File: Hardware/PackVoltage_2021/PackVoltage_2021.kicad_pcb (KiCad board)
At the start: 2 copper layers, 152.4 x 177.8 mm, 139 parts, among them J3V1 Test_Point, J5V1 Test_Point, Q1 BUK7M8R5-40HX, Q10 BUK7M8R5-40HX, Q2 BUK7M8R5-40HX, Q3 BUK7M8R5-40HX, Q4 BUK7M8R5-40HX, Q5 BUK7M8R5-40HX, Q6 BUK7M8R5-40HX, Q7 BUK7M8R5-40HX, Q8 BUK7M8R5-40HX, Q9 BUK7M8R5-40HX, U1 LT1910, U10 INA281, U12 OKI-78SR-3.3_1.5-W36-C, U13 OKI-78SR-5_1.5-W36-C, U14 LT1910, U15 LT1910, U16 LT1910, U17 INA281, U18 INA281, U19 INA281, U2 LT1910, U20 LT1910, U21 LT1910, U22 INA281, U23 INA281, U24 TM4C129E_Launchpad, U3 LT1910, U4 INA281, U5 INA281, U6 INA281, U7 LT1910, U8 LT1910, U9 INA281

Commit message: rearranged components
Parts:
- removed the REF** at (172.7, 67.8)
- removed the REF** at (168.9, 156.7)
- added REF**: 4_40_Hole, MRDT_Drill_Holes:4_40_Hole, F.Cu at (169.4, 63.2)
- added REF**: 4_40_Hole, MRDT_Drill_Holes:4_40_Hole, F.Cu at (169.4, 156.7)
- moved R10 196.0 mm to (168.9, 19.6)
- moved U5 184.2 mm to (156.5, 32.0)
- moved U7 148.9 mm to (176.5, 22.4)
- moved R9 24.2 mm to (100.8, 33.8), turned to 180 degrees
- moved D5 19.6 mm to (100.8, 31.5), turned to 180 degrees
- moved R3 13.5 mm to (93.2, 19.3), turned to 90 degrees
- moved U3 11.2 mm to (102.9, 25.9)
- moved J3V1 8.13 mm to (89.9, 71.1)
- moved Q3 7.37 mm to (110.2, 26.4), turned to 270 degrees
- moved C7 5.45 mm to (95.5, 12.2)
- moved R6 1.61 mm to (114.6, 21.6)
- moved U6 1.61 mm to (104.1, 14.5), turned to 90 degrees
- moved C19 0.80 mm to (83.2, 66.5)
- moved D13 0.80 mm to (82.3, 63.0)
- moved R18 0.80 mm to (83.2, 59.7)
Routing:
- net +3V3: track 137.8 -> 111.5 mm

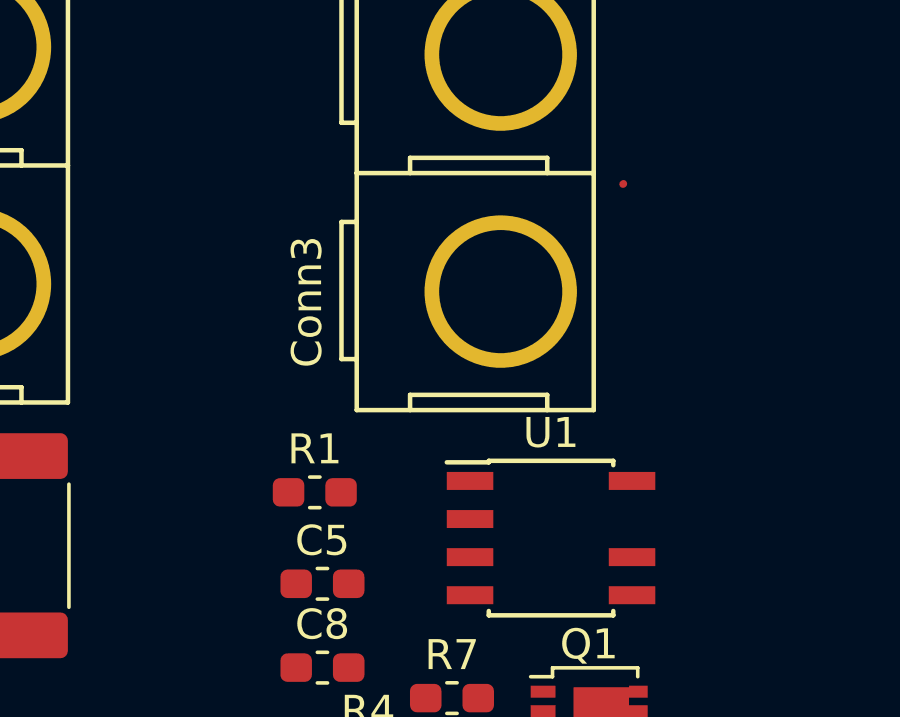
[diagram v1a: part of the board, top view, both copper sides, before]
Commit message: rearranged components (layout)
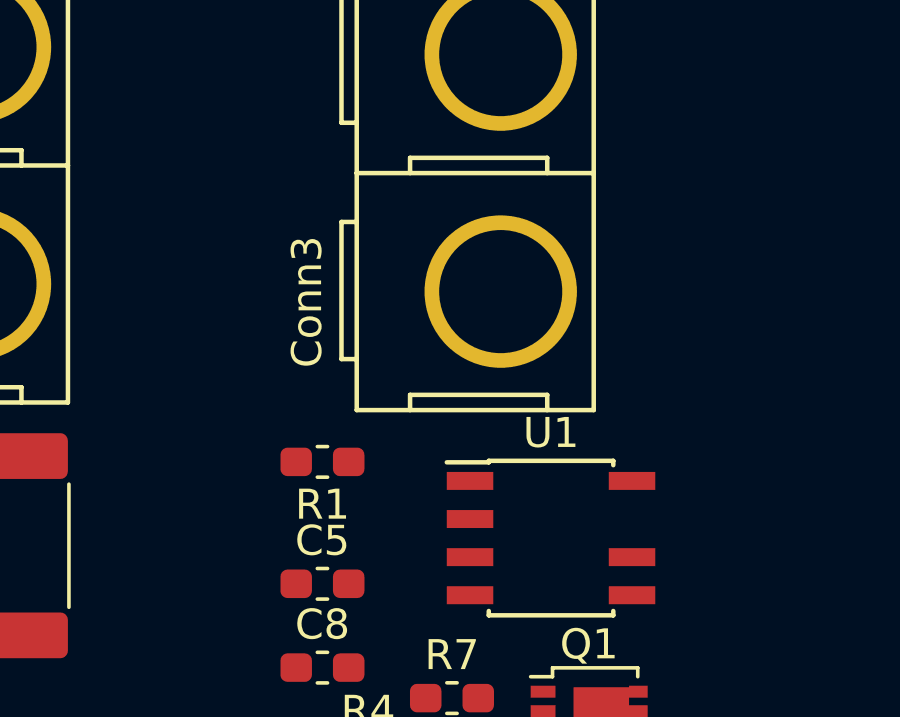
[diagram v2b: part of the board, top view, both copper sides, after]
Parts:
- moved R1 1.05 mm to (124.7, 18.8), turned to 180 degrees

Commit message: circuit, deletes
made circuit to copy across board (hopefully);
deleted old traces that "aren't wide enough"
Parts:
- removed J3V1, J5V1: Test_Point, TestPoint:TestPoint_Pad_2.5x2.5mm
- removed REF** (x4): 4_40_Hole, MRDT_Drill_Holes:4_40_Hole
- moved U4 21.1 mm to (129.3, 14.2), turned to 90 degrees
- moved C8 17.3 mm to (127.8, 42.7), turned to 270 degrees
- moved D3 17.1 mm to (143.0, 17.8), turned to 270 degrees
- moved D5 16.0 mm to (113.5, 21.8), turned to 270 degrees
- moved R4 15.8 mm to (139.4, 21.1), turned to 90 degrees
- moved Conn10 15.3 mm to (208.8, 4.83)
- moved C7 15.2 mm to (102.6, 25.7), turned to 0 degrees
- moved R7 14.9 mm to (143.0, 21.6), turned to 90 degrees
- moved R9 14.8 mm to (112.5, 24.6), turned to 0 degrees
- moved Conn9 10.4 mm to (184.9, 4.83)
- moved U1 8.64 mm to (124.5, 24.9), turned to 270 degrees
- moved Q3 8.29 mm to (106.4, 33.8)
- moved R3 8.18 mm to (99.8, 14.5)
- moved Conn7 7.41 mm to (161.0, 4.83)
- moved C19 7.37 mm to (90.6, 66.3)
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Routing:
- net /DriveCTL: track 125.6 -> 0.00 mm
- net /ExtraCTL: track 123.7 -> 0.00 mm
- net /CameraCTL: track 122.5 -> 0.00 mm
- net /BuckCTL: track 117.5 -> 0.08 mm
- net /NavBoardCTL: track 110.9 -> 0.00 mm
- net /GimbalActCTL: track 110.1 -> 0.00 mm
- net /GimbalLogCTL: track 108.3 -> 0.00 mm
- net /AuxActCTL: track 106.4 -> 0.00 mm
- net /AuxLogCTL: track 104.5 -> 0.00 mm
- net /MultimediaLogCTL: track 103.6 -> 0.90 mm
- net /MultimediaActCTL: track 102.7 -> 0.00 mm
- net /GimbalSense: track 81.9 -> 0.00 mm
- net /LowCurrentSense: track 75.7 -> 0.00 mm
- net +3V3: track 111.5 -> 36.8 mm, vias 0 -> 2
- net /MultimediaSense: track 69.5 -> 0.00 mm
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- added copper zone on F.Cu, net /Anderson_M1
- added copper zone on F.Cu, net /Anderson_M2
- added copper zone on F.Cu, net Net-(C10-Pad1)
- added copper zone on F.Cu, net Net-(Q1-Pad1)
- added copper zone on F.Cu, net Net-(Q3-Pad1)
- removed copper zone on B.Cu, net GND

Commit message: did a thing
arranged circuit for motor 2
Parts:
- moved C13 206.5 mm to (158.5, 42.7), turned to 270 degrees
- moved C29 188.4 mm to (173.0, 42.7), turned to 270 degrees
- moved C9 16.6 mm to (143.5, 42.7), turned to 270 degrees
- moved R4 14.0 mm to (125.5, 21.3)
- moved R7 13.8 mm to (129.5, 24.6), turned to 180 degrees
- moved U4 13.5 mm to (117.1, 20.1)
- moved D3 13.0 mm to (130.6, 21.6)
- moved Q1 12.7 mm to (123.6, 33.8)
- moved Conn3 11.7 mm to (125.5, 4.70)
- moved C5 10.3 mm to (118.6, 25.9), turned to 0 degrees
- moved U1 8.99 mm to (118.4, 31.5)
- moved R1 7.85 mm to (116.6, 14.5)
- moved C8 0.51 mm to (127.3, 42.7)
- moved Q3 0.13 mm to (106.6, 33.8)
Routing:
- net Net-(Q1-Pad4): track 0.00 -> 8.09 mm, vias 0 -> 2
- added copper zone on F.Cu, net (none)
- removed copper zone on F.Cu, net /Anderson_M2
- removed copper zone on F.Cu, net Net-(Q1-Pad1)

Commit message: uhh more circuits
finished top circuits on layout, fixed two resistors in schematic
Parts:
- moved C11 209.8 mm to (153.0, 25.9)
- moved D4 198.9 mm to (146.9, 21.6), turned to 270 degrees
- moved Q4 198.8 mm to (156.5, 33.8), turned to 270 degrees
- moved R14 192.5 mm to (162.1, 24.6)
- moved R28 192.2 mm to (166.1, 14.5), turned to 90 degrees
- moved C27 189.8 mm to (169.4, 25.9)
- moved R32 189.5 mm to (178.6, 24.6)
- moved D17 186.0 mm to (179.6, 21.3), turned to 270 degrees
- moved U9 182.3 mm to (150.4, 20.1), turned to 90 degrees
- moved D6 178.0 mm to (163.1, 21.3), turned to 270 degrees
- moved R12 175.9 mm to (158.0, 21.3), turned to 90 degrees
- moved Q9 166.6 mm to (173.0, 33.8), turned to 270 degrees
- moved U22 166.2 mm to (166.1, 20.1), turned to 90 degrees
- moved R30 162.5 mm to (174.5, 21.3), turned to 90 degrees
- moved U20 161.0 mm to (167.9, 31.5), turned to 270 degrees
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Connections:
- R14 pad 1: /Anderson_M4 -> Net-(Q4-Pad1)
- R32 pad 1: /Anderson_D1 -> Net-(Q9-Pad1)
- U24 pad PD2: /Current_Sensor_M3 -> /Driver_M3
- U24 pad PP0: /Driver_M3 -> /Current_Sensor_M3
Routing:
- net +3V3: track 36.8 -> 137.1 mm, vias 2 -> 7
- net /Current_Sensor_M3: track 0.00 -> 83.4 mm, vias 0 -> 2
- net /Driver_M3: track 0.00 -> 74.6 mm, vias 0 -> 2
- net /Current_Sensor_M2: track 0.00 -> 70.2 mm, vias 0 -> 2
- net +5V: track 25.5 -> 94.9 mm, vias 1 -> 3
- net /Driver_M2: track 0.00 -> 62.0 mm, vias 0 -> 2
- net Net-(R2-Pad1): track 0.00 -> 22.0 mm, vias 0 -> 4
- net Net-(R28-Pad1): track 0.00 -> 21.5 mm, vias 0 -> 4
- net Net-(R1-Pad1): track 0.00 -> 20.4 mm, vias 0 -> 4
- net Net-(R10-Pad1): track 0.00 -> 20.4 mm, vias 0 -> 4
- net Net-(Q9-Pad1): track 0.00 -> 10.7 mm, vias 0 -> 2
- net Net-(Q1-Pad1): track 0.00 -> 10.2 mm, vias 0 -> 2
- net Net-(Q2-Pad1): track 0.00 -> 9.99 mm, vias 0 -> 2
- net Net-(Q4-Pad1): track 0.00 -> 9.62 mm, vias 0 -> 2
- net Net-(Q2-Pad4): track 0.00 -> 7.93 mm, vias 0 -> 2
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- added copper zone on F.Cu, net /Anderson_D1
- added copper zone on F.Cu, net /Anderson_M2
- added copper zone on F.Cu, net /Anderson_M3
- added copper zone on F.Cu, net Net-(C13-Pad1)
- added copper zone on F.Cu, net Net-(C29-Pad1)
- added copper zone on F.Cu, net Net-(C8-Pad1)
- added copper zone on F.Cu, net Net-(C9-Pad1)
- added copper zone on F.Cu, net Net-(Q1-Pad1)
- added copper zone on F.Cu, net Net-(Q2-Pad1)
- added copper zone on F.Cu, net Net-(Q4-Pad1)
- added copper zone on F.Cu, net Net-(Q9-Pad1)

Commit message: circuit work
finished circuit for the spare motor (first one on the right side of the board) to copy across the right side
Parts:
- moved U10 169.8 mm to (211.1, 41.1), turned to 0 degrees
- moved R15 162.3 mm to (202.9, 51.6), turned to 270 degrees
- moved C12 149.5 mm to (199.8, 37.6)
- moved U8 149.5 mm to (193.5, 38.1), turned to 270 degrees
- moved D7 146.1 mm to (205.9, 52.6), turned to 180 degrees
- moved Q5 145.8 mm to (200.7, 45.2), turned to 180 degrees
- moved R11 142.2 mm to (207.0, 38.6), turned to 90 degrees
- moved R13 113.7 mm to (211.6, 46.5)
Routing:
- net +5V: track 94.9 -> 216.1 mm, vias 3 -> 8
- net /Current_Sensor_S1: track 0.00 -> 55.4 mm, vias 0 -> 2
- net Net-(R11-Pad1): track 0.00 -> 17.9 mm, vias 0 -> 2
- net Net-(Q5-Pad4): track 0.00 -> 13.9 mm, vias 0 -> 2
- net Net-(C12-Pad1): track 0.00 -> 6.84 mm, vias 0 -> 2
- net Net-(Q5-Pad1): track 0.00 -> 4.85 mm
- net Net-(D7-Pad2): track 0.00 -> 2.10 mm
- added copper zone on F.Cu, net /Anderson_M4
- added copper zone on F.Cu, net /Anderson_S1
- added copper zone on F.Cu, net Net-(C14-Pad1)
- added copper zone on F.Cu, net Net-(Q5-Pad1)
- removed copper zone on F.Cu, net (none)

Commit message: finished circuits
finished main circuits
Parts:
- moved R17 241.4 mm to (187.5, 175.0), turned to 180 degrees
- moved D12 239.8 mm to (191.5, 175.0), turned to 180 degrees
- moved C26 177.8 mm to (199.1, 140.0), turned to 270 degrees
- moved U16 173.1 mm to (193.5, 126.5), turned to 270 degrees
- moved R21 167.9 mm to (206.0, 126.7)
- moved C23 167.8 mm to (199.4, 125.5)
- moved Q6 167.5 mm to (200.7, 111.5), turned to 180 degrees
- moved C25 165.5 mm to (199.9, 74.9), turned to 270 degrees
- moved R19 163.6 mm to (207.0, 105.2), turned to 90 degrees
- moved C21 162.1 mm to (199.6, 104.1)
- moved C22 160.8 mm to (199.4, 61.0)
- moved R29 160.0 mm to (206.2, 83.8)
- moved Q8 160.0 mm to (200.7, 133.1), turned to 180 degrees
- moved R27 159.0 mm to (202.7, 140.0), turned to 270 degrees
- moved Q10 157.1 mm to (200.9, 89.7), turned to 180 degrees
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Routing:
- net +5V: track 216.1 -> 449.3 mm, vias 8 -> 24
- net /Current_Sensor_T1: track 0.00 -> 113.9 mm, vias 0 -> 6
- net /Current_Sensor_V1: track 0.00 -> 80.0 mm, vias 0 -> 4
- net /Current_Sensor_M4: track 0.00 -> 74.4 mm, vias 0 -> 2
- net /Current_Sensor_A1: track 0.00 -> 67.5 mm, vias 0 -> 4
- net /Driver_S1: track 0.00 -> 64.9 mm, vias 0 -> 4
- net /Current_Sensor_R1: track 0.00 -> 64.0 mm, vias 0 -> 4
- net /Driver_M4: track 0.00 -> 63.0 mm, vias 0 -> 2
- net /Current_Sensor_D1: track 0.00 -> 60.8 mm
- net /Driver_T1: track 0.00 -> 55.8 mm, vias 0 -> 2
- net /Driver_D1: track 0.00 -> 53.5 mm
- net /Driver_V1: track 0.00 -> 50.0 mm, vias 0 -> 2
- net /Driver_R1: track 0.00 -> 39.8 mm, vias 0 -> 2
- net /Driver_A1: track 0.00 -> 33.7 mm, vias 0 -> 2
- net /Current_Sensor_S1: track 55.4 -> 89.0 mm, vias 2 -> 4
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- added copper zone on F.Cu, net /Anderson_A1
- added copper zone on F.Cu, net /Anderson_R1
- added copper zone on F.Cu, net /Anderson_T1
- added copper zone on F.Cu, net /Anderson_V1
- added copper zone on B.Cu, net GND
- added copper zone on F.Cu, net Net-(C24-Pad1)
- added copper zone on F.Cu, net Net-(C25-Pad1)
- added copper zone on F.Cu, net Net-(C26-Pad1)
- added copper zone on F.Cu, net Net-(C30-Pad1)
- added copper zone on F.Cu, net Net-(Q10-Pad1)
- added copper zone on F.Cu, net Net-(Q6-Pad1)
- added copper zone on F.Cu, net Net-(Q7-Pad1)
- added copper zone on F.Cu, net Net-(Q8-Pad1)

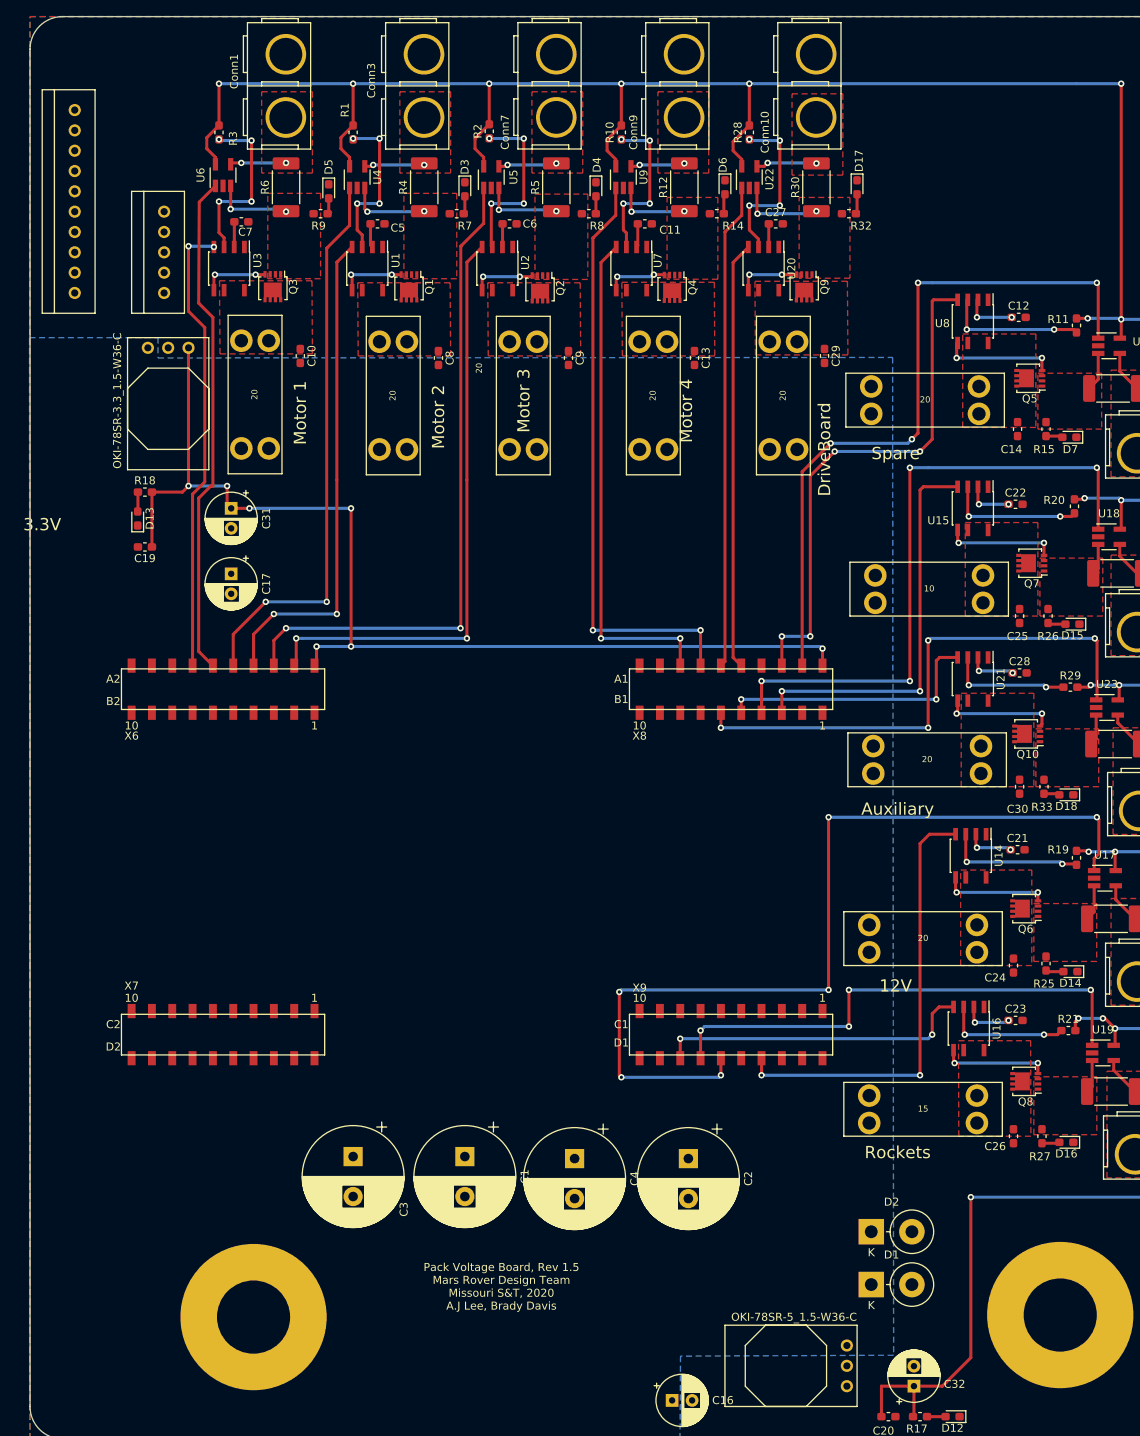
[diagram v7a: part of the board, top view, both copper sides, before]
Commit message: molexes
- changed 5 pin molex to 4 pin molex (removed buckCTL)
- started making traces from molexes to tiva
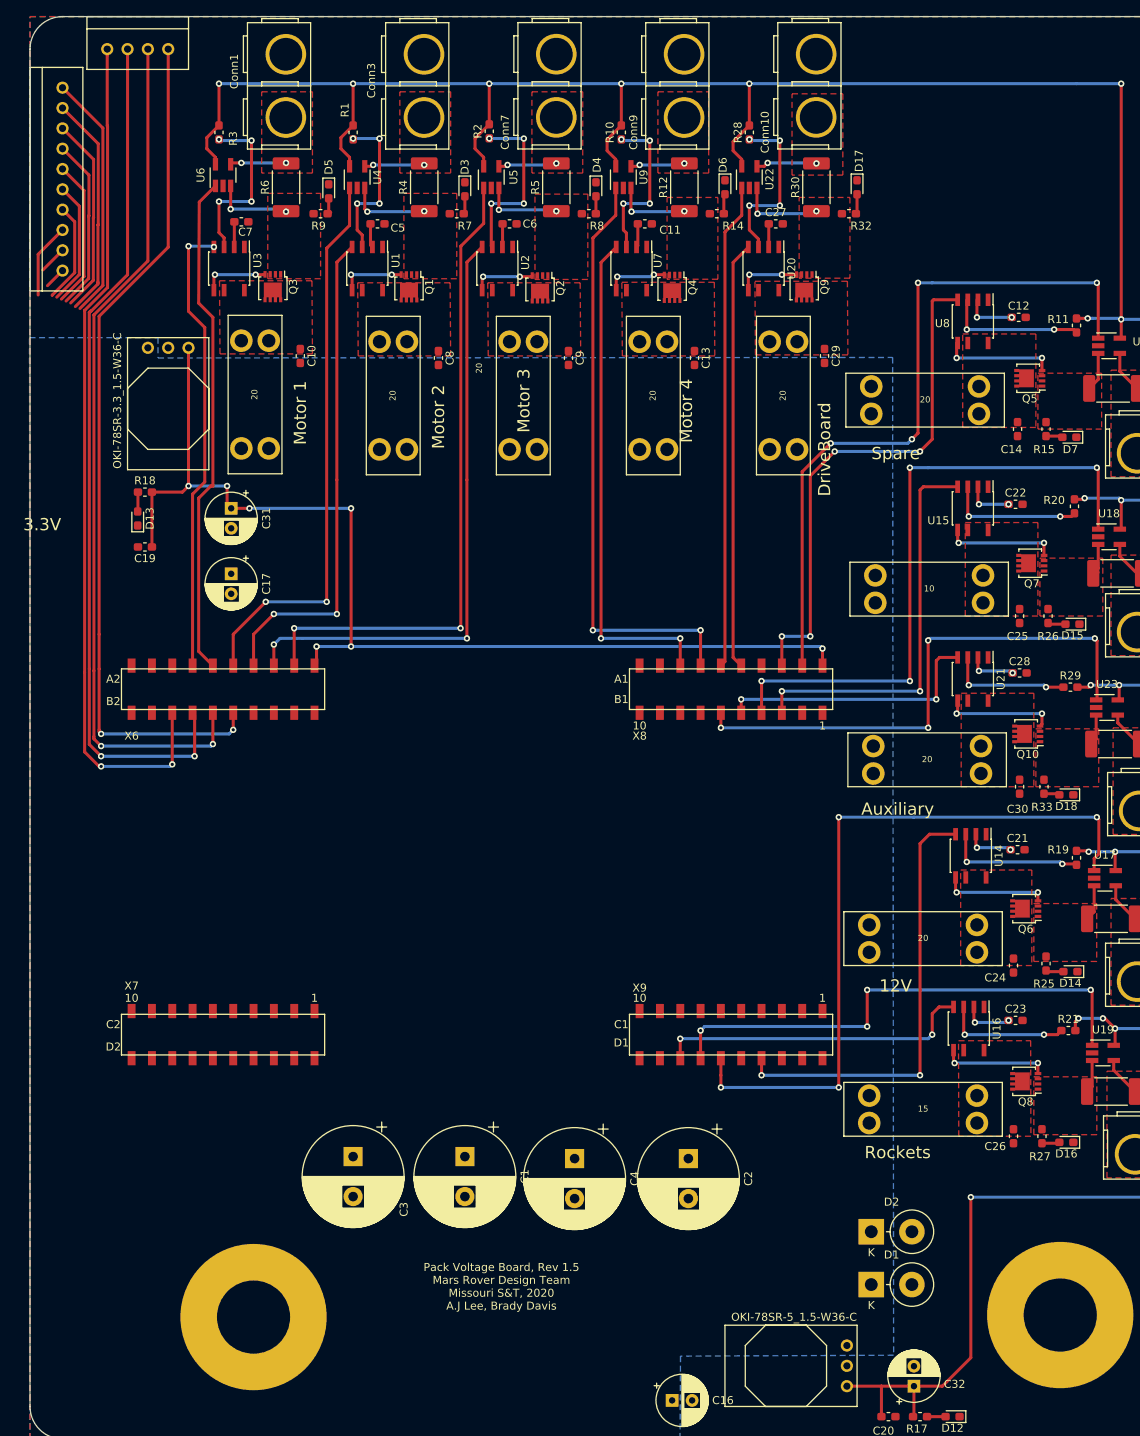
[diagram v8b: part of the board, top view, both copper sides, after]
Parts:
- Conn6: value Molex_SL_05 -> Molex_SL_04; footprint MRDT_Connectors:MOLEX_SL_05_Vertical -> MRDT_Connectors:MOLEX_SL_04_Vertical
- moved Conn6 31.3 mm to (85.9, 4.06), turned to 0 degrees
- moved Conn5 3.18 mm to (80.3, 31.8)
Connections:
- Conn1 pad 2: /Anderson_M1 -> (no net)
- Conn10 pad 2: /Anderson_D1 -> (no net)
- Conn11 pad 2: /Anderson_A1 -> (no net)
- Conn12 pad 2: /Anderson_S1 -> (no net)
- Conn2 pad 2: /Anderson_R1 -> (no net)
- Conn3 pad 2: /Anderson_M2 -> (no net)
- Conn4 pad 2: /Anderson_T1 -> (no net)
- Conn7 pad 2: /Anderson_M3 -> (no net)
- Conn8 pad 2: /Anderson_V1 -> (no net)
- Conn9 pad 2: /Anderson_M4 -> (no net)
- U24 pad PD2: /Driver_M3 -> /Current_Sensor_M3
- U24 pad PG1: /BuckCTL -> Net-(U24-PadPG1)
- U24 pad PP0: /Current_Sensor_M3 -> /Driver_M3
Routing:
- net /LowCurrentSense: track 0.00 -> 108.3 mm, vias 0 -> 2
- net /MultimediaSense: track 0.00 -> 108.3 mm, vias 0 -> 2
- net /GimbalSense: track 0.00 -> 108.1 mm, vias 0 -> 2
- net /AuxMountSense: track 0.00 -> 107.3 mm, vias 0 -> 2
- net /DriveCTL: track 0.00 -> 30.9 mm
- net /ExtraCTL: track 0.00 -> 27.9 mm
- net /CameraCTL: track 0.00 -> 24.6 mm
- net /Current_Sensor_T1: track 113.9 -> 92.0 mm, vias 6 -> 4
- net /NavBoardCTL: track 0.00 -> 21.6 mm
- net /GimbalActCTL: track 0.00 -> 18.5 mm
- net /GimbalLogCTL: track 0.00 -> 15.5 mm
- net /AuxActCTL: track 0.00 -> 12.5 mm
- net /AuxLogCTL: track 0.00 -> 9.39 mm
- net +5V: track 449.3 -> 453.6 mm
- net /MultimediaActCTL: track 0.00 -> 3.49 mm
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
